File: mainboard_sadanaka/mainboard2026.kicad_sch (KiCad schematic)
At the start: 48 parts, among them J1 Conn_01x06, J10 Conn_01x06_Pin, J11 Conn_01x02_Pin, J12 Conn_01x02_Pin, J2 Conn_01x06, J3 Conn_02x08_Counter_Clockwise, J4 Conn_01x02, J5 Conn_01x02, J7 Conn_01x02, J8 Conn_01x03_Pin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

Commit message: 回路図を更新
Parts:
- removed C11: 4.7u, Capacitor_SMD:C_0603_1608Metric_Pad1.08x0.95mm_HandSolder, symbol Device:C
- removed D1, D2, D3: LED, LED_THT:LED_D3.0mm, symbol Device:LED
- removed J3: Conn_02x08_Counter_Clockwise, Package_SO:SOP-16_4.4x10.4mm_P1.27mm, symbol Connector_Generic:Conn_02x08_Counter_Clockwise
- removed J4: Conn_01x02, Connector_JST:JST_PH_B2B-PH-K_1x02_P2.00mm_Vertical, symbol Connector_Generic:Conn_01x02
- removed R7: 100k, Resistor_SMD:R_0603_1608Metric_Pad0.98x0.95mm_HandSolder, symbol Device:R
- removed R8: 4.7R, Resistor_SMD:R_0603_1608Metric_Pad0.98x0.95mm_HandSolder, symbol Device:R
- added C7: 0.1u, Capacitor_SMD:C_0603_1608Metric_Pad1.08x0.95mm_HandSolder, symbol Device:C
- added J6: Conn_01x02, Connector_JST:JST_PH_B2B-PH-K_1x02_P2.00mm_Vertical, symbol Connector_Generic:Conn_01x02
- added U8: CH340N, Package_SO:SOP-8_3.9x4.9mm_P1.27mm, symbol Interface_USB:CH340N
- added U9: MCP3002, symbol Analog_ADC:MCP3002
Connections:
- net DM2: now also J6.2 (Pin_2), U8.2 (UD-)
- net DP2: now also J6.1 (Pin_1), U8.1 (UD+)
- net GND: now also C7.1, U8.3 (GND), U9.4 (VSS)
- net LORA_RX: now also U8.6 (TXD)
- net LORA_TX: now also U8.7 (RXD)
- net VCC: now also C7.2, U8.5 (VCC), U8.8 (V3); no longer U11.1 (3V3), U11.17 (3V3__1)
- net SPI0_SCLK: now reaches U11.23 (GPIO11/SPI_SCLK)
- net SPI0_SCLK: now also U9.7 (CLK)
- net SPI0_MISO: now reaches U11.21 (GPIO9/SPI_MISO)
- net SPI0_MISO: now also U9.6 (DOUT)
- net SPI0_MOSI: now reaches U11.19 (GPIO10/SPI_MOSI)
- net SPI0_MOSI: now also U9.5 (DIN)
- net SPI0_CE0: now reaches U11.24 (GPIO8/~{SPI_CE0})
- net SPI0_CE0: now also U9.1 (~{CS}/SHDN)
- new net ADC_CH0: U9.2 (CH0)
- new net ANALOG: U9.3 (CH1)
- new net POWER: U11.1 (3V3), U11.17 (3V3__1), U9.8 (VDD/VREF)
- no-connect marks 59 -> 54
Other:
- note added: "rasberrypiに直接はんだ付け"

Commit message: 回路図を更新
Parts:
- removed C5: 0.1u, Capacitor_SMD:C_0603_1608Metric_Pad1.08x0.95mm_HandSolder, symbol Device:C
- removed U4: CH340N, Package_SO:SOP-8_3.9x4.9mm_P1.27mm, symbol Interface_USB:CH340N
- added J3: Conn_01x02_Pin, Connector_JST:JST_PH_B2B-PH-K_1x02_P2.00mm_Vertical, symbol Connector:Conn_01x02_Pin
- added R4: 10k, Resistor_SMD:R_0603_1608Metric_Pad0.98x0.95mm_HandSolder, symbol Device:R
- added R5: 1k, Resistor_SMD:R_0603_1608Metric_Pad0.98x0.95mm_HandSolder, symbol Device:R
- J10, J9: footprint (none) -> Connector_JST:JST_XH_S6B-XH-A-1_1x06_P2.50mm_Horizontal
- J11, J12: footprint (none) -> Connector_JST:JST_PH_B2B-PH-K_1x02_P2.00mm_Vertical
- J8: footprint (none) -> Connector:FanPinHeader_1x03_P2.54mm_Vertical
- U9: footprint (none) -> PCM_Package_DIP_AKL:DIP-8_W7.62mm
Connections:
- net ANALOG: now also J3.2 (Pin_2), R4.2
- net GND: now also R4.1
- net ADC_CH0: no longer names the net of U9.2 (CH0)
- net POWER renamed 3V3
- net 3V3: now also R5.1
- new net: J3.1 (Pin_1), R5.2

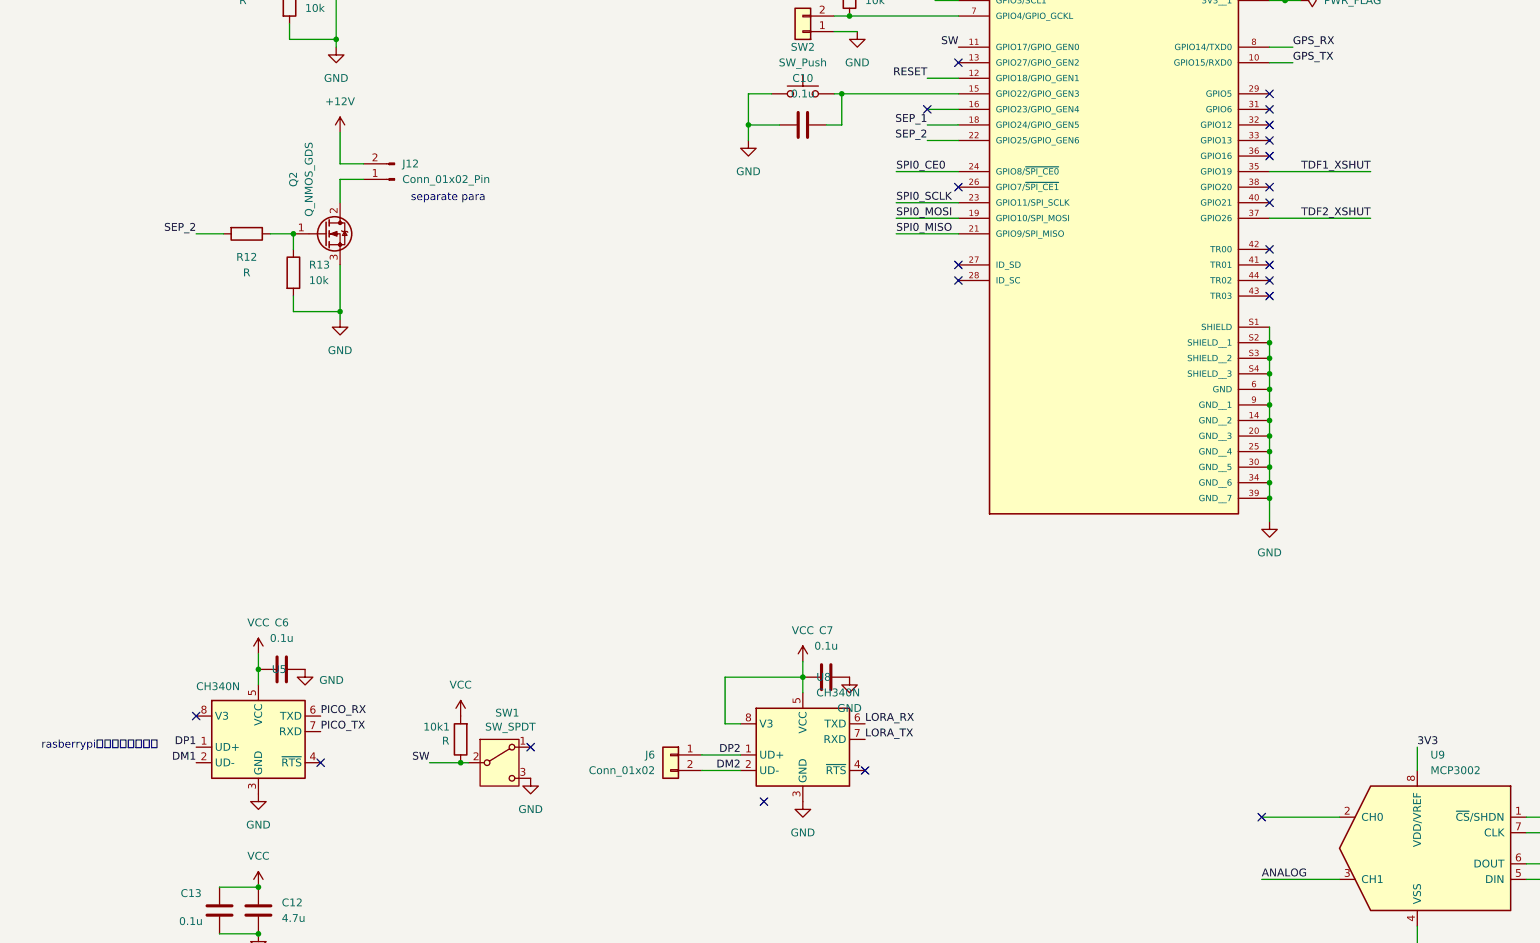
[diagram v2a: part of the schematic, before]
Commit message: KiCadプロジェクトを更新
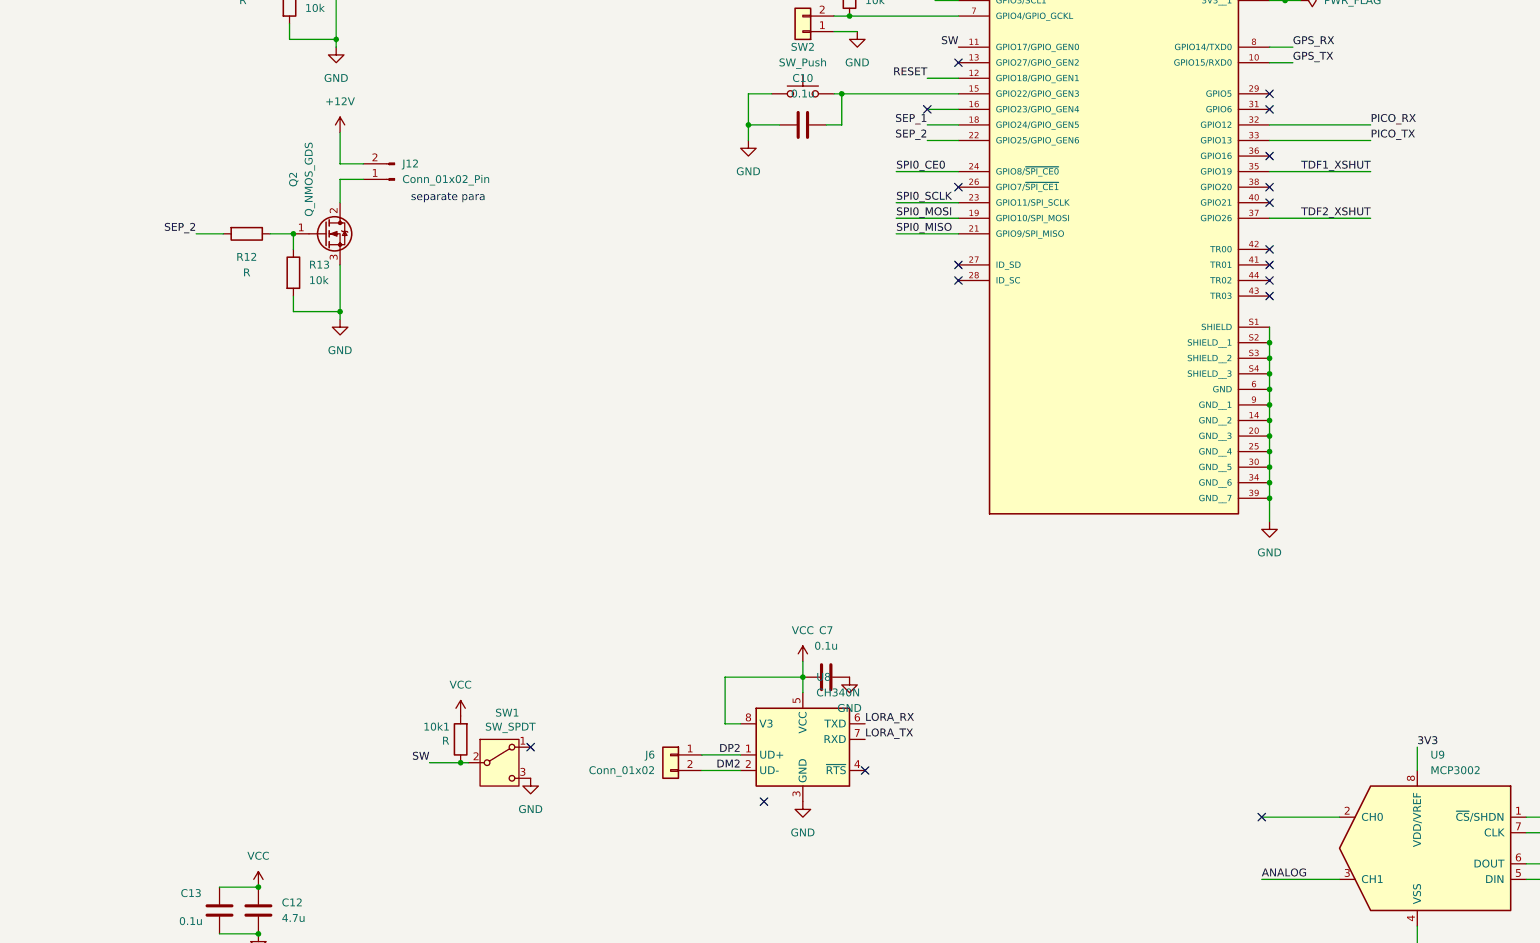
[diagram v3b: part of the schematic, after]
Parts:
- removed C6: 0.1u, Capacitor_SMD:C_0603_1608Metric_Pad1.08x0.95mm_HandSolder, symbol Device:C
- removed U5: CH340N, Package_SO:SOP-8_3.9x4.9mm_P1.27mm, symbol Interface_USB:CH340N
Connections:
- net PICO_RX: now also U11.32 (GPIO12)
- net PICO_TX: now also U11.33 (GPIO13)
- no-connect marks 54 -> 50
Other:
- note removed: "rasberrypiに直接はんだ付け"
